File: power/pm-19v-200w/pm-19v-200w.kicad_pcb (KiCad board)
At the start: 4 copper layers, 58.4 x 22.9 mm, 58 parts, among them J1 Brick 1/8 (DOSA), J2 Aux, Q1 BSC070N10NS5, Q2 BSC070N10NS5, Q3 BSC070N10NS5, Q4 BSC070N10NS5, U1 LTC7810, U2 MCP65R46-1.21, U3 MCP65R46-1.21

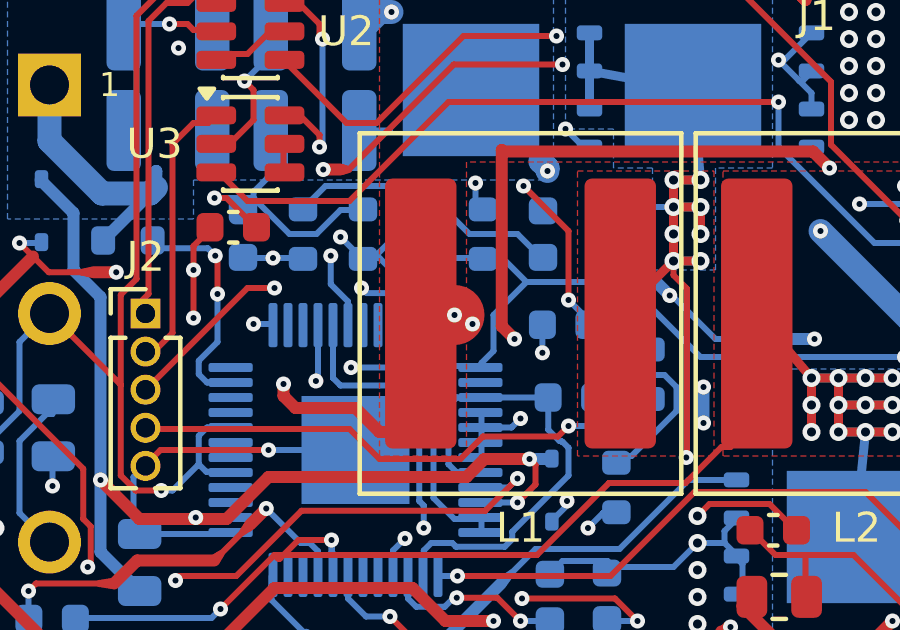
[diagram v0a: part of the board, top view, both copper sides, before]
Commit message: pm-19v-200w: via-in-pad check; drop the redundant SNS1P plane-tap via inside L1.2
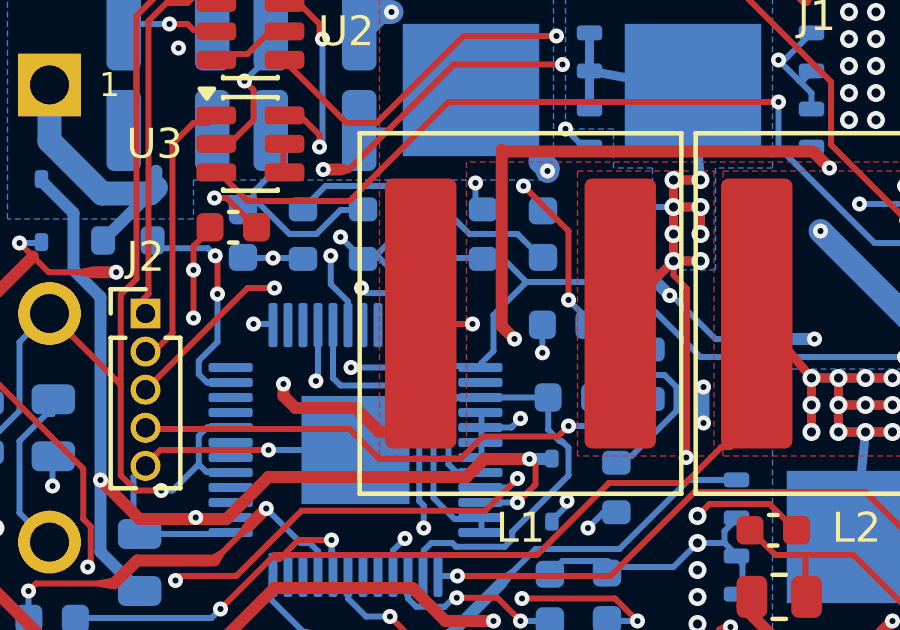
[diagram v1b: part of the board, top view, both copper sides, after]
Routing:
- net /SNS1P: track 37.6 -> 35.6 mm, vias 4 -> 3
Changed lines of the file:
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@@
-	)
-	(segment
-		(start 117.3 111.5)
-		(end 117 111.5)
-		(width 2)
-		(layer "F.Cu")
-		(net "/SNS1P")
 	)
 	(segment
@@
 	)
 	(via
-		(at 117.3 111.5)
-		(size 0.5)
-		(drill 0.2)
-		(layers "F.Cu" "B.Cu")
-		(capping yes)
-		(filling yes)
-		(net "/SNS1P")
-	)
-	(via
 		(at 111.6 113.8)
 		(size 0.5)
@@
 	)
 	(segment
-		(start 117.3 111.5)
-		(end 117.3 111.8)
-		(width 0.2)
-		(layer "B.Cu")
-		(net "/SNS1P")
-	)
-	(segment
 		(start 117.9 111.8)
 		(end 116.8 111.8)
-		(width 0.2)
-		(layer "B.Cu")
-		(net "/SNS1P")
-	)
-	(segment
-		(start 117.3 111.5)
-		(end 116.75 111.8375)
 		(width 0.2)
 		(layer "B.Cu")
@@
 		(layer "In2.Cu")
 		(net "/SNS1P")
-	)
-	(segment
-		(start 117.6 111.5)
-		(end 117.3 111.5)
-		(width 2)
-		(layer "In2.Cu")
-		(net "/SNS1P")
-	)
-	(segment
-		(start 117.9 111.8)
-		(end 117.6 111.5)
-		(width 2)
-		(layer "In2.Cu")
-		(net "/SNS1P")

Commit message: pm-19v-200w: large 19 V silk legend on both sides (L1 ref moved up); handoff: 24 V variant recipe
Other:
- board text added: "19 V"
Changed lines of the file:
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@@
 		(tags "xal")
 		(property "Reference" "L1"
-			(at 0 -7.145 0)
+			(at 0 6.95 0)
 			(layer "F.SilkS")
 			(effects
@@
 		(layer "Edge.Cuts")
 	)
+	(gr_text "19 V"
+		(at 117.6 120 0)
+		(layer "F.SilkS")
+		(effects
+			(font
+				(size 3.2 4.2)
+				(thickness 0.5)
+				(bold yes)
+			)
+		)
+	)
+	(gr_text "19 V"
+		(at 144.3 113.3 0)
+		(layer "B.SilkS")
+		(effects
+			(font
+				(size 2.8 3.6)
+				(thickness 0.45)
+				(bold yes)
+			)
+			(justify mirror)
+		)
+	)
 	(segment

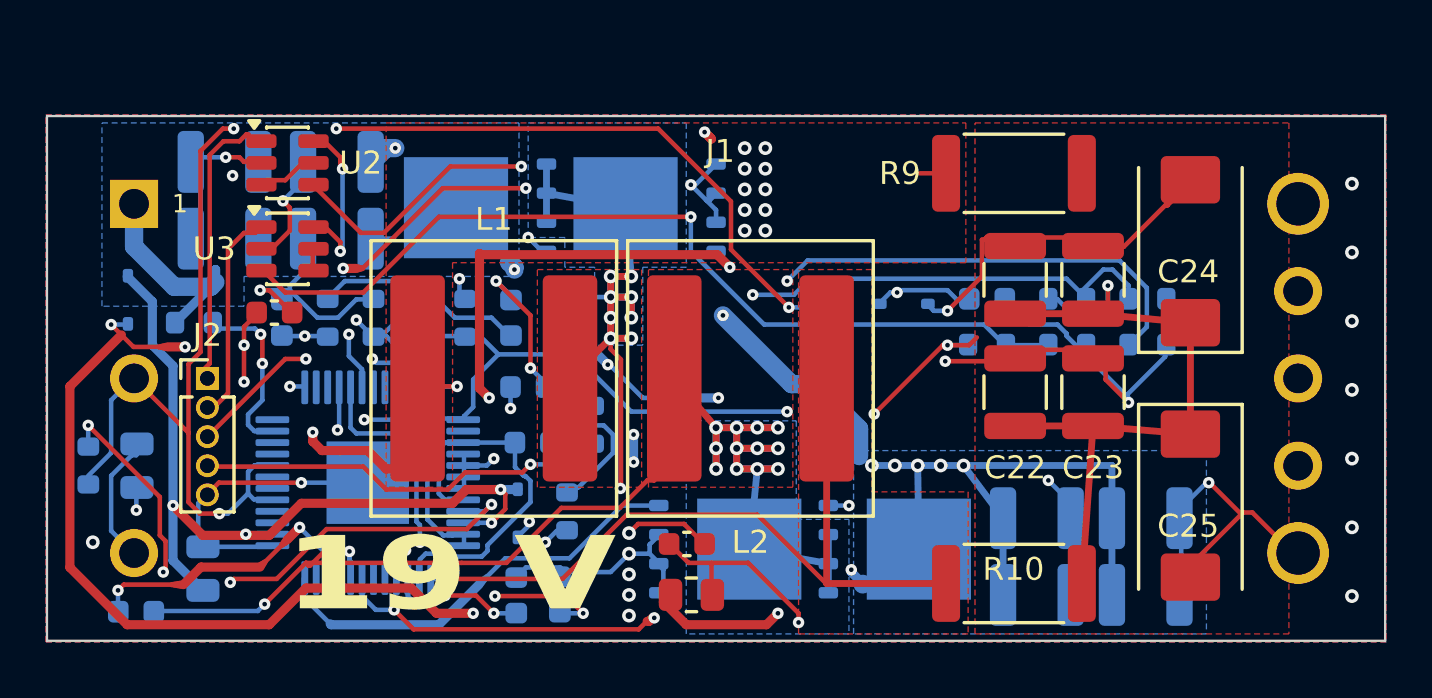
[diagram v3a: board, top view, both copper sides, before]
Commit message: power: screwed PM module mount footprints (M2 into SMT standoffs, pogo aux) on module, plane and bench carrier; RUN moves to aux pad 8; copper not yet rerouted
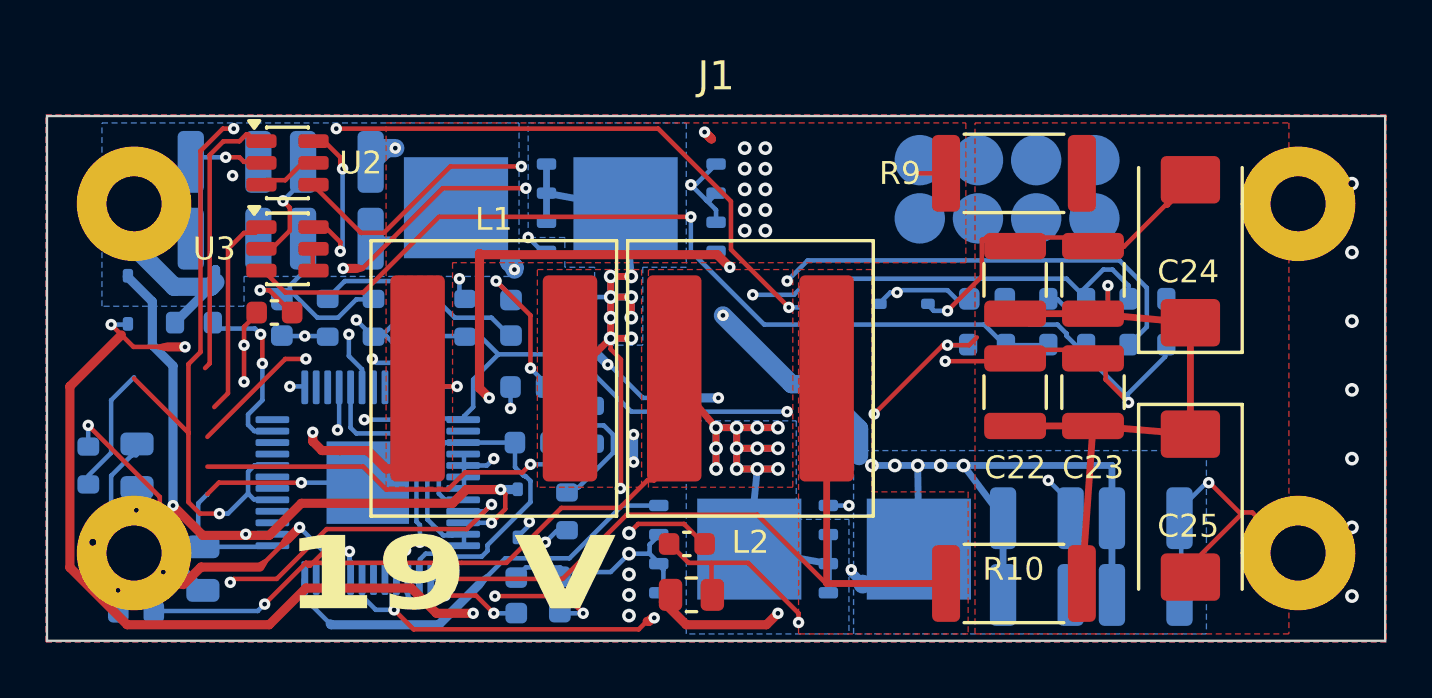
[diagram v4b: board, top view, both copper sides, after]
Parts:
- J1: value Brick 1/8 (DOSA) -> PM mount M2; footprint pm:Brick_Eighth_DOSA -> pm:PM_Mount_M2
- J2: value Aux -> Aux pads (pogo); footprint Connector_PinHeader_1.27mm:PinHeader_1x05_P1.27mm_Vertical -> pm:PM_Aux_Pads_2x04
- moved J2 35.9 mm to (141.9, 103.2)
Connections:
- J1 pad 2: /RUN -> GND
- J1 pad 4: GND -> /VOUT
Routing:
- net GND: vias 36 -> 34
- net /VOUT: vias 4 -> 6

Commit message: Revert "power: screwed PM module mount footprints (M2 into SMT standoffs, pogo aux) on module, plane and bench carrier; RUN moves to aux pad 8; copper not yet rerouted"
This reverts commit abb9f50ba34d0b63e5425fa3cd376420f2890e7d.
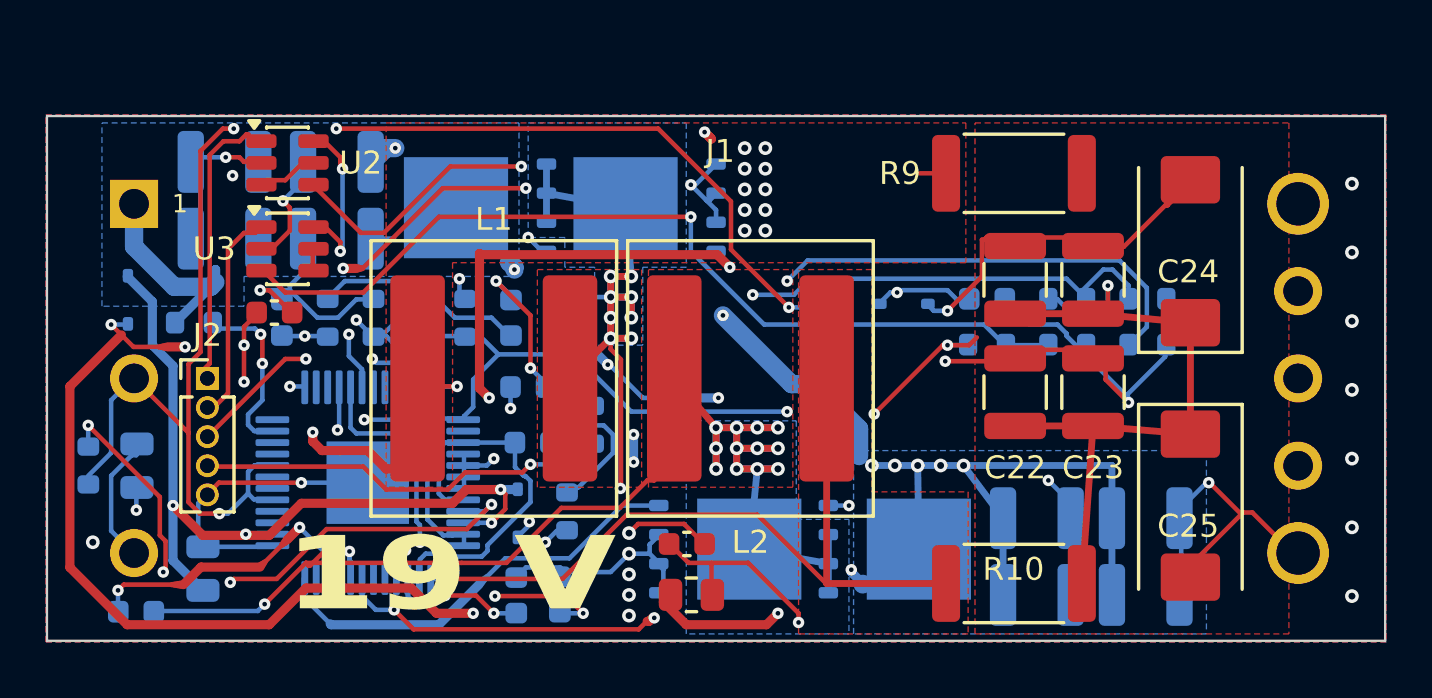
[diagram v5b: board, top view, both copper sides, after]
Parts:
- J1: value PM mount M2 -> Brick 1/8 (DOSA); footprint pm:PM_Mount_M2 -> pm:Brick_Eighth_DOSA
- J2: value Aux pads (pogo) -> Aux; footprint pm:PM_Aux_Pads_2x04 -> Connector_PinHeader_1.27mm:PinHeader_1x05_P1.27mm_Vertical
- moved J2 35.9 mm to (107.0, 111.5)
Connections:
- J1 pad 2: GND -> /RUN
- J1 pad 4: /VOUT -> GND
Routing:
- net GND: vias 34 -> 36
- net /VOUT: vias 6 -> 4
